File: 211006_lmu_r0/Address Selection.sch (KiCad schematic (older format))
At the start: 8 parts

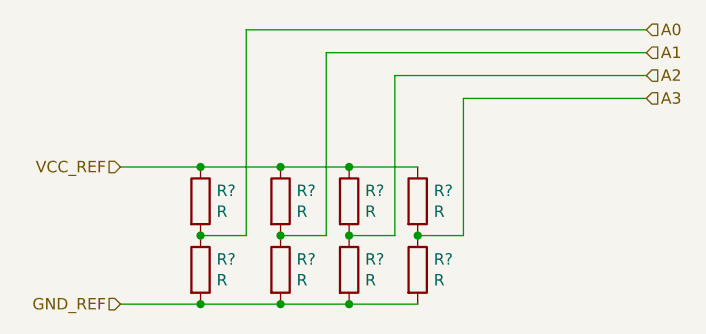
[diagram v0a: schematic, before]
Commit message: Updated BOM and footprints for non-hv components
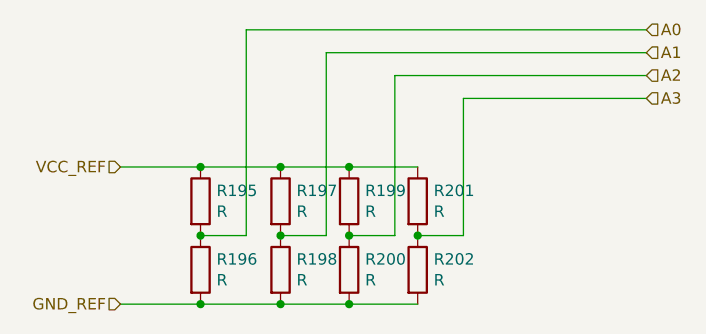
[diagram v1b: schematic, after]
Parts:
- removed R? (x3): R, symbol Device:R
- added R199, R200, R202: R, symbol Device:R
- gave numbers to parts that had none: 5
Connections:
- net A2: now also R199.2, R200.1
- net A3: now also R202.1
- net GND_REF: now also R200.2, R202.2
- net VCC_REF: now also R199.1
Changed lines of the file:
@@
 AR Path="/61619F34/62135562/61FF994E" Ref="R?"  Part="1"
 AR Path="/61619F34/62140E50/61FF994E" Ref="R?"  Part="1"
-AR Path="/61619F34/6215FBD7/61FF994E" Ref="R?"  Part="1"
-F 0 "R?" H 5070 3696 50  0000 L CNN
+AR Path="/61619F34/6215FBD7/61FF994E" Ref="R195"  Part="1"
+F 0 "R195" H 5070 3696 50  0000 L CNN
 F 1 "R" H 5070 3605 50  0000 L CNN
 F 2 "" V 4930 3650 50  0001 C CNN
@@
 AR Path="/61619F34/62135562/61FFA5B8" Ref="R?"  Part="1"
 AR Path="/61619F34/62140E50/61FFA5B8" Ref="R?"  Part="1"
-AR Path="/61619F34/6215FBD7/61FFA5B8" Ref="R?"  Part="1"
-F 0 "R?" H 5070 3996 50  0000 L CNN
+AR Path="/61619F34/6215FBD7/61FFA5B8" Ref="R196"  Part="1"
+F 0 "R196" H 5070 3996 50  0000 L CNN
 F 1 "R" H 5070 3905 50  0000 L CNN
 F 2 "" V 4930 3950 50  0001 C CNN
@@
 AR Path="/61619F34/62135562/6234DD26" Ref="R?"  Part="1"
 AR Path="/61619F34/62140E50/6234DD26" Ref="R?"  Part="1"
-AR Path="/61619F34/6215FBD7/6234DD26" Ref="R?"  Part="1"
-F 0 "R?" H 5420 3696 50  0000 L CNN
+AR Path="/61619F34/6215FBD7/6234DD26" Ref="R197"  Part="1"
+F 0 "R197" H 5420 3696 50  0000 L CNN
 F 1 "R" H 5420 3605 50  0000 L CNN
 F 2 "" V 5280 3650 50  0001 C CNN
@@
 AR Path="/61619F34/62135562/6234DD27" Ref="R?"  Part="1"
 AR Path="/61619F34/62140E50/6234DD27" Ref="R?"  Part="1"
-AR Path="/61619F34/6215FBD7/6234DD27" Ref="R?"  Part="1"
-F 0 "R?" H 5420 3996 50  0000 L CNN
+AR Path="/61619F34/6215FBD7/6234DD27" Ref="R198"  Part="1"
+F 0 "R198" H 5420 3996 50  0000 L CNN
 F 1 "R" H 5420 3905 50  0000 L CNN
 F 2 "" V 5280 3950 50  0001 C CNN
@@
 $Comp
 L Device:R R?
-U 1 1 61FFB654
+U 1 1 61F42E7A
 P 5650 3650
-AR Path="/61619F34/61FF949C/61FFB654" Ref="R?"  Part="1"
-AR Path="/61619F34/620A15AD/61FFB654" Ref="R?"  Part="1"
-AR Path="/61619F34/620DEAEE/61FFB654" Ref="R?"  Part="1"
-AR Path="/61619F34/62127D2E/61FFB654" Ref="R?"  Part="1"
-AR Path="/61619F34/62135562/61FFB654" Ref="R?"  Part="1"
-AR Path="/61619F34/62140E50/61FFB654" Ref="R?"  Part="1"
-AR Path="/61619F34/6215FBD7/61FFB654" Ref="R?"  Part="1"
-F 0 "R?" H 5720 3696 50  0000 L CNN
+AR Path="/61619F34/61FF949C/61F42E7A" Ref="R?"  Part="1"
+AR Path="/61619F34/620A15AD/61F42E7A" Ref="R?"  Part="1"
+AR Path="/61619F34/620DEAEE/61F42E7A" Ref="R?"  Part="1"
+AR Path="/61619F34/62127D2E/61F42E7A" Ref="R?"  Part="1"
+AR Path="/61619F34/62135562/61F42E7A" Ref="R?"  Part="1"
+AR Path="/61619F34/62140E50/61F42E7A" Ref="R?"  Part="1"
+AR Path="/61619F34/6215FBD7/61F42E7A" Ref="R199"  Part="1"
+F 0 "R199" H 5720 3696 50  0000 L CNN
 F 1 "R" H 5720 3605 50  0000 L CNN
 F 2 "" V 5580 3650 50  0001 C CNN
@@
 $Comp
 L Device:R R?
-U 1 1 61FFB65A
+U 1 1 61F42E7B
 P 5650 3950
-AR Path="/61619F34/61FF949C/61FFB65A" Ref="R?"  Part="1"
-AR Path="/61619F34/620A15AD/61FFB65A" Ref="R?"  Part="1"
-AR Path="/61619F34/620DEAEE/61FFB65A" Ref="R?"  Part="1"
-AR Path="/61619F34/62127D2E/61FFB65A" Ref="R?"  Part="1"
-AR Path="/61619F34/62135562/61FFB65A" Ref="R?"  Part="1"
-AR Path="/61619F34/62140E50/61FFB65A" Ref="R?"  Part="1"
-AR Path="/61619F34/6215FBD7/61FFB65A" Ref="R?"  Part="1"
-F 0 "R?" H 5720 3996 50  0000 L CNN
+AR Path="/61619F34/61FF949C/61F42E7B" Ref="R?"  Part="1"
+AR Path="/61619F34/620A15AD/61F42E7B" Ref="R?"  Part="1"
+AR Path="/61619F34/620DEAEE/61F42E7B" Ref="R?"  Part="1"
+AR Path="/61619F34/62127D2E/61F42E7B" Ref="R?"  Part="1"
+AR Path="/61619F34/62135562/61F42E7B" Ref="R?"  Part="1"
+AR Path="/61619F34/62140E50/61F42E7B" Ref="R?"  Part="1"
+AR Path="/61619F34/6215FBD7/61F42E7B" Ref="R200"  Part="1"
+F 0 "R200" H 5720 3996 50  0000 L CNN
 F 1 "R" H 5720 3905 50  0000 L CNN
 F 2 "" V 5580 3950 50  0001 C CNN
@@
 AR Path="/61619F34/62135562/61FFBB96" Ref="R?"  Part="1"
 AR Path="/61619F34/62140E50/61FFBB96" Ref="R?"  Part="1"
-AR Path="/61619F34/6215FBD7/61FFBB96" Ref="R?"  Part="1"
-F 0 "R?" H 6020 3696 50  0000 L CNN
+AR Path="/61619F34/6215FBD7/61FFBB96" Ref="R201"  Part="1"
+F 0 "R201" H 6020 3696 50  0000 L CNN
 F 1 "R" H 6020 3605 50  0000 L CNN
 F 2 "" V 5880 3650 50  0001 C CNN
@@
 $Comp
 L Device:R R?
-U 1 1 61FFBB9C
+U 1 1 61F42E7D
 P 5950 3950
-AR Path="/61619F34/61FF949C/61FFBB9C" Ref="R?"  Part="1"
-AR Path="/61619F34/620A15AD/61FFBB9C" Ref="R?"  Part="1"
-AR Path="/61619F34/620DEAEE/61FFBB9C" Ref="R?"  Part="1"
-AR Path="/61619F34/62127D2E/61FFBB9C" Ref="R?"  Part="1"
-AR Path="/61619F34/62135562/61FFBB9C" Ref="R?"  Part="1"
-AR Path="/61619F34/62140E50/61FFBB9C" Ref="R?"  Part="1"
-AR Path="/61619F34/6215FBD7/61FFBB9C" Ref="R?"  Part="1"
-F 0 "R?" H 6020 3996 50  0000 L CNN
+AR Path="/61619F34/61FF949C/61F42E7D" Ref="R?"  Part="1"
+AR Path="/61619F34/620A15AD/61F42E7D" Ref="R?"  Part="1"
+AR Path="/61619F34/620DEAEE/61F42E7D" Ref="R?"  Part="1"
+AR Path="/61619F34/62127D2E/61F42E7D" Ref="R?"  Part="1"
+AR Path="/61619F34/62135562/61F42E7D" Ref="R?"  Part="1"
+AR Path="/61619F34/62140E50/61F42E7D" Ref="R?"  Part="1"
+AR Path="/61619F34/6215FBD7/61F42E7D" Ref="R202"  Part="1"
+F 0 "R202" H 6020 3996 50  0000 L CNN
 F 1 "R" H 6020 3905 50  0000 L CNN
 F 2 "" V 5880 3950 50  0001 C CNN

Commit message: Cleaned up last components missing footprint refs
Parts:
- R195, R196, R197, R198, R199, R200, R201, R202: footprint (none) -> Resistor_SMD:R_0603_1608Metric_Pad0.98x0.95mm_HandSolder
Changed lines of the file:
@@
 F 0 "R195" H 5070 3696 50  0000 L CNN
 F 1 "R" H 5070 3605 50  0000 L CNN
-F 2 "" V 4930 3650 50  0001 C CNN
+F 2 "Resistor_SMD:R_0603_1608Metric_Pad0.98x0.95mm_HandSolder" V 4930 3650 50  0001 C CNN
 F 3 "~" H 5000 3650 50  0001 C CNN
 	1    5000 3650
@@
 F 0 "R196" H 5070 3996 50  0000 L CNN
 F 1 "R" H 5070 3905 50  0000 L CNN
-F 2 "" V 4930 3950 50  0001 C CNN
+F 2 "Resistor_SMD:R_0603_1608Metric_Pad0.98x0.95mm_HandSolder" V 4930 3950 50  0001 C CNN
 F 3 "~" H 5000 3950 50  0001 C CNN
 	1    5000 3950
@@
 F 0 "R197" H 5420 3696 50  0000 L CNN
 F 1 "R" H 5420 3605 50  0000 L CNN
-F 2 "" V 5280 3650 50  0001 C CNN
+F 2 "Resistor_SMD:R_0603_1608Metric_Pad0.98x0.95mm_HandSolder" V 5280 3650 50  0001 C CNN
 F 3 "~" H 5350 3650 50  0001 C CNN
 	1    5350 3650
@@
 F 0 "R198" H 5420 3996 50  0000 L CNN
 F 1 "R" H 5420 3905 50  0000 L CNN
-F 2 "" V 5280 3950 50  0001 C CNN
+F 2 "Resistor_SMD:R_0603_1608Metric_Pad0.98x0.95mm_HandSolder" V 5280 3950 50  0001 C CNN
 F 3 "~" H 5350 3950 50  0001 C CNN
 	1    5350 3950
@@
 F 0 "R199" H 5720 3696 50  0000 L CNN
 F 1 "R" H 5720 3605 50  0000 L CNN
-F 2 "" V 5580 3650 50  0001 C CNN
+F 2 "Resistor_SMD:R_0603_1608Metric_Pad0.98x0.95mm_HandSolder" V 5580 3650 50  0001 C CNN
 F 3 "~" H 5650 3650 50  0001 C CNN
 	1    5650 3650
@@
 F 0 "R200" H 5720 3996 50  0000 L CNN
 F 1 "R" H 5720 3905 50  0000 L CNN
-F 2 "" V 5580 3950 50  0001 C CNN
+F 2 "Resistor_SMD:R_0603_1608Metric_Pad0.98x0.95mm_HandSolder" V 5580 3950 50  0001 C CNN
 F 3 "~" H 5650 3950 50  0001 C CNN
 	1    5650 3950
@@
 F 0 "R201" H 6020 3696 50  0000 L CNN
 F 1 "R" H 6020 3605 50  0000 L CNN
-F 2 "" V 5880 3650 50  0001 C CNN
+F 2 "Resistor_SMD:R_0603_1608Metric_Pad0.98x0.95mm_HandSolder" V 5880 3650 50  0001 C CNN
 F 3 "~" H 5950 3650 50  0001 C CNN
 	1    5950 3650
@@
 F 0 "R202" H 6020 3996 50  0000 L CNN
 F 1 "R" H 6020 3905 50  0000 L CNN
-F 2 "" V 5880 3950 50  0001 C CNN
+F 2 "Resistor_SMD:R_0603_1608Metric_Pad0.98x0.95mm_HandSolder" V 5880 3950 50  0001 C CNN
 F 3 "~" H 5950 3950 50  0001 C CNN
 	1    5950 3950

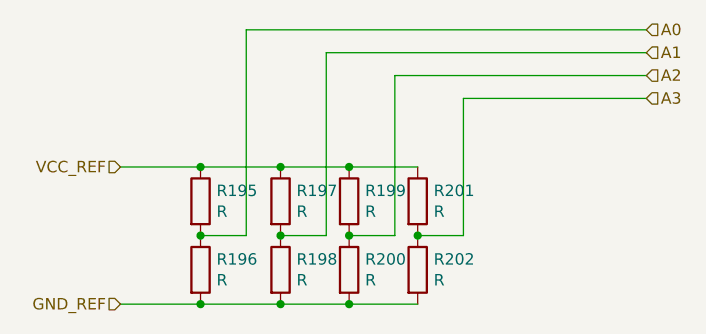
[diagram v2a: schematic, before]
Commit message: Updated with Mouser links for BOM
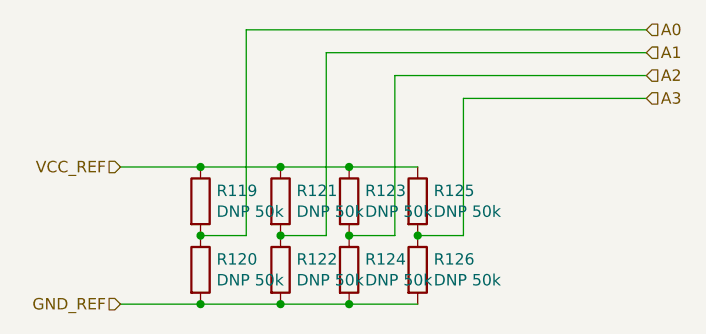
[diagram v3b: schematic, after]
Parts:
- R119: renamed from R195; value R -> DNP 50k
- R120: renamed from R196; value R -> DNP 50k
- R121: renamed from R197; value R -> DNP 50k
- R122: renamed from R198; value R -> DNP 50k
- R123: renamed from R199; value R -> DNP 50k
- R124: renamed from R200; value R -> DNP 50k
- R125: renamed from R201; value R -> DNP 50k
- R126: renamed from R202; value R -> DNP 50k
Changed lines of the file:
@@
 AR Path="/61619F34/62135562/61FF994E" Ref="R?"  Part="1"
 AR Path="/61619F34/62140E50/61FF994E" Ref="R?"  Part="1"
-AR Path="/61619F34/6215FBD7/61FF994E" Ref="R195"  Part="1"
-F 0 "R195" H 5070 3696 50  0000 L CNN
-F 1 "R" H 5070 3605 50  0000 L CNN
+AR Path="/61619F34/6215FBD7/61FF994E" Ref="R119"  Part="1"
+F 0 "R119" H 5070 3696 50  0000 L CNN
+F 1 "DNP 50k" H 5070 3605 50  0000 L CNN
 F 2 "Resistor_SMD:R_0603_1608Metric_Pad0.98x0.95mm_HandSolder" V 4930 3650 50  0001 C CNN
 F 3 "~" H 5000 3650 50  0001 C CNN
@@
 AR Path="/61619F34/62135562/61FFA5B8" Ref="R?"  Part="1"
 AR Path="/61619F34/62140E50/61FFA5B8" Ref="R?"  Part="1"
-AR Path="/61619F34/6215FBD7/61FFA5B8" Ref="R196"  Part="1"
-F 0 "R196" H 5070 3996 50  0000 L CNN
-F 1 "R" H 5070 3905 50  0000 L CNN
+AR Path="/61619F34/6215FBD7/61FFA5B8" Ref="R120"  Part="1"
+F 0 "R120" H 5070 3996 50  0000 L CNN
+F 1 "DNP 50k" H 5070 3905 50  0000 L CNN
 F 2 "Resistor_SMD:R_0603_1608Metric_Pad0.98x0.95mm_HandSolder" V 4930 3950 50  0001 C CNN
 F 3 "~" H 5000 3950 50  0001 C CNN
@@
 AR Path="/61619F34/62135562/6234DD26" Ref="R?"  Part="1"
 AR Path="/61619F34/62140E50/6234DD26" Ref="R?"  Part="1"
-AR Path="/61619F34/6215FBD7/6234DD26" Ref="R197"  Part="1"
-F 0 "R197" H 5420 3696 50  0000 L CNN
-F 1 "R" H 5420 3605 50  0000 L CNN
+AR Path="/61619F34/6215FBD7/6234DD26" Ref="R121"  Part="1"
+F 0 "R121" H 5420 3696 50  0000 L CNN
+F 1 "DNP 50k" H 5420 3605 50  0000 L CNN
 F 2 "Resistor_SMD:R_0603_1608Metric_Pad0.98x0.95mm_HandSolder" V 5280 3650 50  0001 C CNN
 F 3 "~" H 5350 3650 50  0001 C CNN
@@
 AR Path="/61619F34/62135562/6234DD27" Ref="R?"  Part="1"
 AR Path="/61619F34/62140E50/6234DD27" Ref="R?"  Part="1"
-AR Path="/61619F34/6215FBD7/6234DD27" Ref="R198"  Part="1"
-F 0 "R198" H 5420 3996 50  0000 L CNN
-F 1 "R" H 5420 3905 50  0000 L CNN
+AR Path="/61619F34/6215FBD7/6234DD27" Ref="R122"  Part="1"
+F 0 "R122" H 5420 3996 50  0000 L CNN
+F 1 "DNP 50k" H 5420 3905 50  0000 L CNN
 F 2 "Resistor_SMD:R_0603_1608Metric_Pad0.98x0.95mm_HandSolder" V 5280 3950 50  0001 C CNN
 F 3 "~" H 5350 3950 50  0001 C CNN
@@
 AR Path="/61619F34/62135562/61F42E7A" Ref="R?"  Part="1"
 AR Path="/61619F34/62140E50/61F42E7A" Ref="R?"  Part="1"
-AR Path="/61619F34/6215FBD7/61F42E7A" Ref="R199"  Part="1"
-F 0 "R199" H 5720 3696 50  0000 L CNN
-F 1 "R" H 5720 3605 50  0000 L CNN
+AR Path="/61619F34/6215FBD7/61F42E7A" Ref="R123"  Part="1"
+F 0 "R123" H 5720 3696 50  0000 L CNN
+F 1 "DNP 50k" H 5720 3605 50  0000 L CNN
 F 2 "Resistor_SMD:R_0603_1608Metric_Pad0.98x0.95mm_HandSolder" V 5580 3650 50  0001 C CNN
 F 3 "~" H 5650 3650 50  0001 C CNN
@@
 AR Path="/61619F34/62135562/61F42E7B" Ref="R?"  Part="1"
 AR Path="/61619F34/62140E50/61F42E7B" Ref="R?"  Part="1"
-AR Path="/61619F34/6215FBD7/61F42E7B" Ref="R200"  Part="1"
-F 0 "R200" H 5720 3996 50  0000 L CNN
-F 1 "R" H 5720 3905 50  0000 L CNN
+AR Path="/61619F34/6215FBD7/61F42E7B" Ref="R124"  Part="1"
+F 0 "R124" H 5720 3996 50  0000 L CNN
+F 1 "DNP 50k" H 5720 3905 50  0000 L CNN
 F 2 "Resistor_SMD:R_0603_1608Metric_Pad0.98x0.95mm_HandSolder" V 5580 3950 50  0001 C CNN
 F 3 "~" H 5650 3950 50  0001 C CNN
@@
 AR Path="/61619F34/62135562/61FFBB96" Ref="R?"  Part="1"
 AR Path="/61619F34/62140E50/61FFBB96" Ref="R?"  Part="1"
-AR Path="/61619F34/6215FBD7/61FFBB96" Ref="R201"  Part="1"
-F 0 "R201" H 6020 3696 50  0000 L CNN
-F 1 "R" H 6020 3605 50  0000 L CNN
+AR Path="/61619F34/6215FBD7/61FFBB96" Ref="R125"  Part="1"
+F 0 "R125" H 6020 3696 50  0000 L CNN
+F 1 "DNP 50k" H 6020 3605 50  0000 L CNN
 F 2 "Resistor_SMD:R_0603_1608Metric_Pad0.98x0.95mm_HandSolder" V 5880 3650 50  0001 C CNN
 F 3 "~" H 5950 3650 50  0001 C CNN
@@
 AR Path="/61619F34/62135562/61F42E7D" Ref="R?"  Part="1"
 AR Path="/61619F34/62140E50/61F42E7D" Ref="R?"  Part="1"
-AR Path="/61619F34/6215FBD7/61F42E7D" Ref="R202"  Part="1"
-F 0 "R202" H 6020 3996 50  0000 L CNN
-F 1 "R" H 6020 3905 50  0000 L CNN
+AR Path="/61619F34/6215FBD7/61F42E7D" Ref="R126"  Part="1"
+F 0 "R126" H 6020 3996 50  0000 L CNN
+F 1 "DNP 50k" H 6020 3905 50  0000 L CNN
 F 2 "Resistor_SMD:R_0603_1608Metric_Pad0.98x0.95mm_HandSolder" V 5880 3950 50  0001 C CNN
 F 3 "~" H 5950 3950 50  0001 C CNN
